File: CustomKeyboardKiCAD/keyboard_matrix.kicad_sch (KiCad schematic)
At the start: 198 parts, among them SW1 SW_Push, SW10 SW_Push, SW100 SW_Push, SW101 SW_Push, SW102 SW_Push, SW103 SW_Push, SW104 SW_Push, SW105 SW_Push, SW106 SW_Push, SW108 SW_Push, SW11 SW_Push, SW12 SW_Push, SW13 SW_Push, SW14 SW_Push, SW19 SW_Push, SW2 SW_Push, SW20 SW_Push, SW21 SW_Push, SW22 SW_Push, SW23 SW_Push, SW24 SW_Push, SW25 SW_Push, SW26 SW_Push, SW27 SW_Push, SW28 SW_Push, SW29 SW_Push, SW3 SW_Push, SW30 SW_Push, SW31 SW_Push, SW32 SW_Push, SW33 SW_Push, SW34 SW_Push, SW35 SW_Push, SW36 SW_Push, SW37 SW_Push, SW38 SW_Push, SW39 SW_Push, SW4 SW_Push, SW40 SW_Push, SW41 SW_Push, SW42 SW_Push, SW43 SW_Push, SW44 SW_Push, SW45 SW_Push, SW46 SW_Push, SW47 SW_Push, SW48 SW_Push, SW49 SW_Push, SW5 SW_Push, SW50 SW_Push, SW51 SW_Push, SW52 SW_Push, SW53 SW_Push, SW54 SW_Push, SW55 SW_Push, SW56 SW_Push, SW57 SW_Push, SW58 SW_Push, SW59 SW_Push, SW6 SW_Push, SW60 SW_Push, SW61 SW_Push, SW62 SW_Push, SW63 SW_Push, SW64 SW_Push, SW65 SW_Push, SW66 SW_Push, SW67 SW_Push, SW68 SW_Push, SW69 SW_Push, SW7 SW_Push, SW70 SW_Push, SW71 SW_Push, SW72 SW_Push, SW73 SW_Push, SW74 SW_Push, SW75 SW_Push, SW76 SW_Push, SW77 SW_Push, SW78 SW_Push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

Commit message: schematic is generally complete
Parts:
- D10, D11, D12, D13, D14, D15, D16, D186, D187, D188, D190, D191, D193, D194, D195, D196, D197, D198, D199, D200, D202, D21, D22, D23, D24, D25, D26, D27, D28, D29, D3, D30, D31, D32, D33, D34, D35, D36, D37, D38, D39, D4, D40, D41, D42, D43, D44, D45, D46, D47, D48, D49, D5, D50, D51, D52, D53, D54, D55, D56, D57, D58, D59, D6, D60, D61, D62, D63, D64, D65, D66, D67, D68, D69, D7, D70, D71, D72, D73, D74, D75, D76, D77, D78, D79, D8, D80, D81, D82, D83, D84, D85, D86, D88, D89, D9, D90, D91, D92: footprint (none) -> 1N4148W:SODFL3816X120N

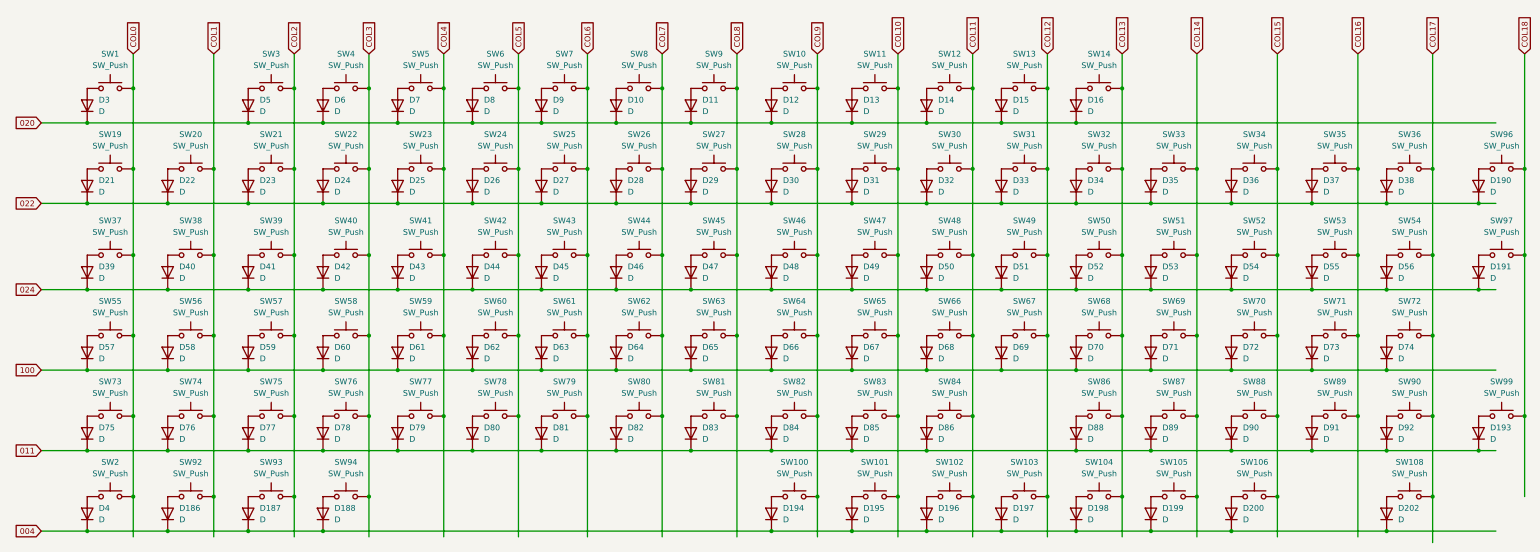
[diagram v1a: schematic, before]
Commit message: major progress on pcb, schematic complete
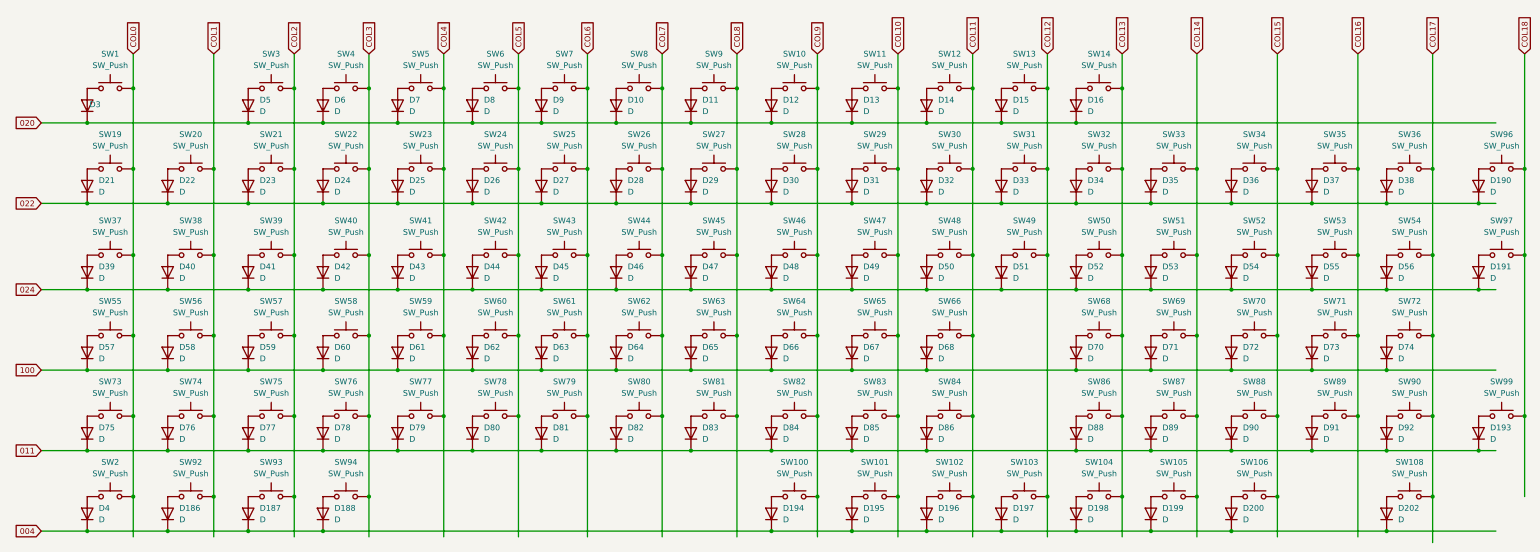
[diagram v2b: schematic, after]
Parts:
- removed D69: D, 1N4148W:SODFL3816X120N, symbol Device:D
- removed SW67: SW_Push, ai03:MX-Hotswap-1U, symbol Switch:SW_Push
- D10, D11, D12, D13, D14, D15, D16, D186, D187, D188, D190, D191, D193, D194, D195, D196, D197, D198, D199, D200, D202, D21, D22, D23, D24, D25, D26, D27, D28, D29, D3, D30, D31, D32, D33, D34, D35, D36, D37, D38, D39, D4, D40, D41, D42, D43, D44, D45, D46, D47, D48, D49, D5, D50, D51, D52, D53, D54, D55, D56, D57, D58, D59, D6, D60, D61, D62, D63, D64, D65, D66, D67, D68, D7, D70, D71, D72, D73, D74, D75, D76, D77, D78, D79, D8, D80, D81, D82, D83, D84, D85, D86, D88, D89, D9, D90, D91, D92: footprint 1N4148W:SODFL3816X120N -> Diode_SMD:D_SOD-123
- SW84: footprint ai03:MX-Hotswap-2.25U -> ai03:MX-Hotswap-1.75U

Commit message: pcb complete
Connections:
- net 004 renamed 104
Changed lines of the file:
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@@
+		)
+	)
+	(global_label "104"
+		(shape input)
+		(at 60.96 154.94 180)
+		(fields_autoplaced yes)
+		(effects
+			(font
+				(size 1.27 1.27)
+			)
+			(justify right)
+		)
+		(property "Intersheetrefs" "${INTERSHEET_REFS}"
+			(at 54.3463 154.94 0)
+			(effects
+				(font
+					(size 1.27 1.27)
+				)
+				(justify right)
+				(hide yes)
+			)
 		)
 	)
@@
 			(effects
 				(font
-					(size 1.27 1.27)
-				)
-				(justify right)
-				(hide yes)
-			)
-		)
-	)
-	(global_label "004"
-		(shape input)
-		(at 60.96 154.94 180)
-		(fields_autoplaced yes)
-		(effects
-			(font
-				(size 1.27 1.27)
-			)
-			(justify right)
-		)
-		(property "Intersheetrefs" "${INTERSHEET_REFS}"
-			(at 54.3463 154.94 0)
-			(effects
-				(font
